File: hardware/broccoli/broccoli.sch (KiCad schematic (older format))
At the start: 82 parts, among them J1 PCB Antenna, J2 USB-MICRO-B, P1 DIGITAL, P11 SCLK, P12 SDAT, P2 PROGRAM, P3 JTAG, P4 EXPAND, P5 ANALOG, P6 VCC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

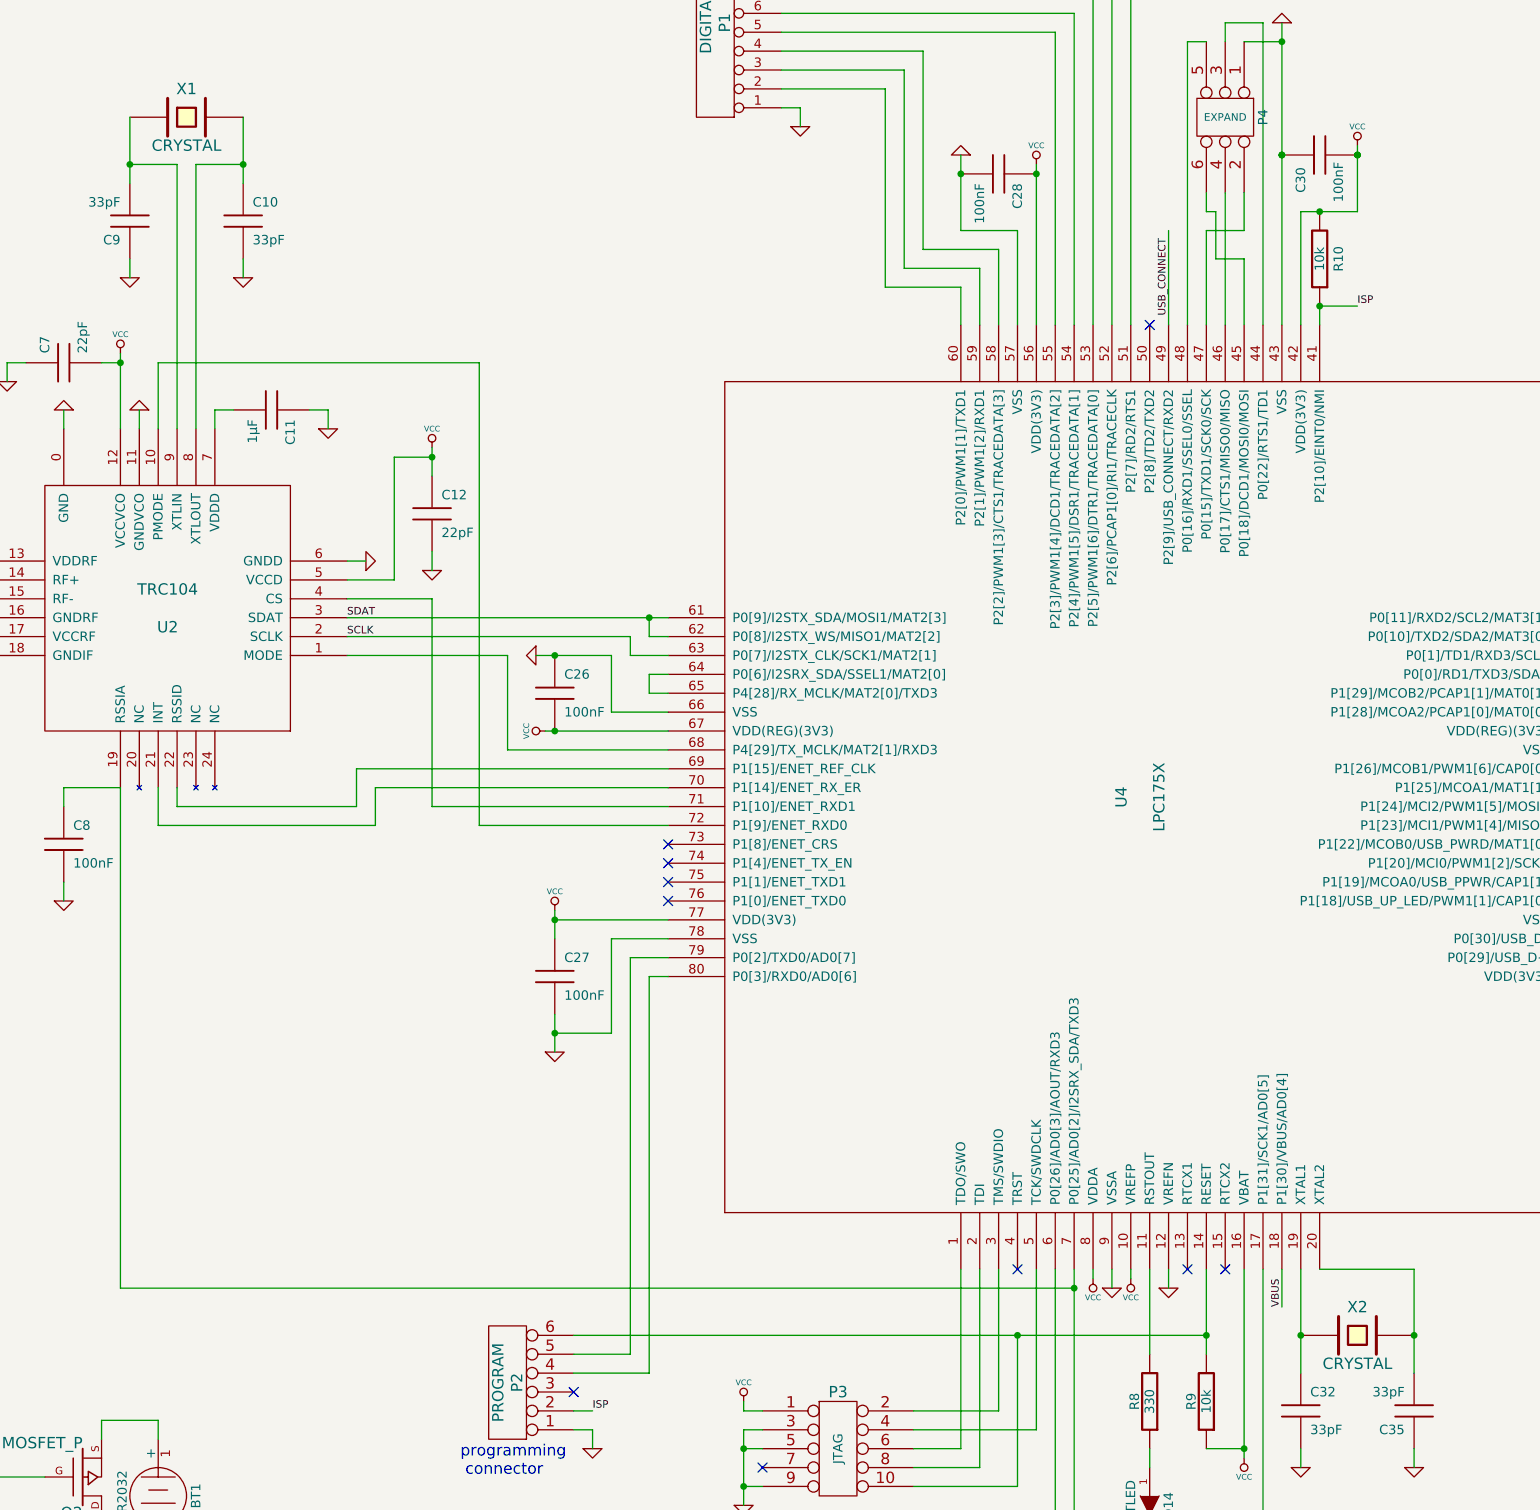
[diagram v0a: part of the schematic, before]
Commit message: Broccoli: replaced some bogus modules
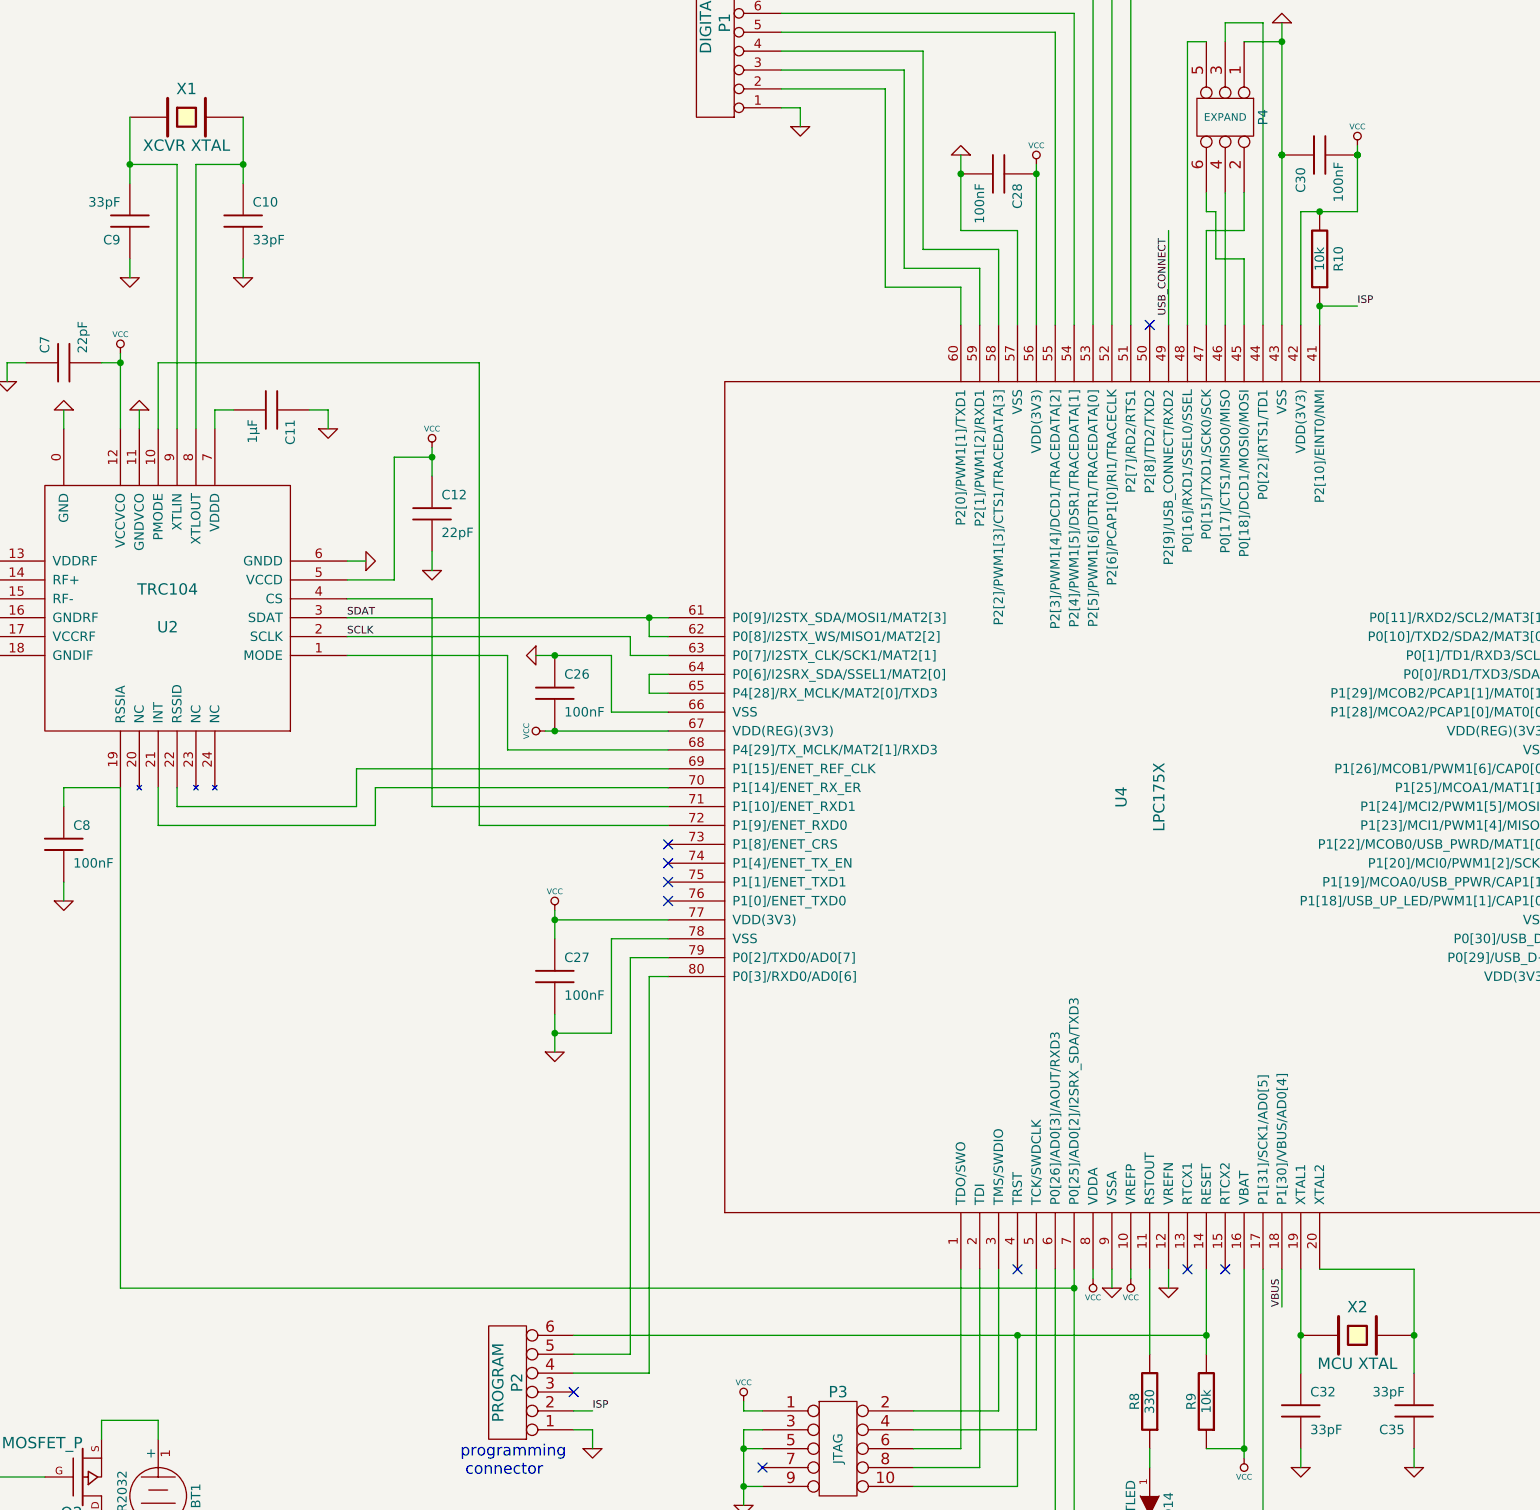
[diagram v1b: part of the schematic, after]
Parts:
- X1: value CRYSTAL -> XCVR XTAL
- X2: value CRYSTAL -> MCU XTAL
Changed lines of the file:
@@
-EESchema Schematic File Version 2  date Sat 13 Aug 2011 10:34:51 PM MDT
+EESchema Schematic File Version 2  date Sun 14 Aug 2011 11:25:26 AM MDT
 LIBS:ubertooth-symbols
 LIBS:power
@@
 P 4750 2000
 F 0 "X1" H 4750 2150 60  0000 C CNN
-F 1 "CRYSTAL" H 4750 1850 60  0000 C CNN
+F 1 "XCVR XTAL" H 4750 1850 60  0000 C CNN
 F 4 "TXC" H 4750 2000 60  0001 C CNN "Field1"
 F 5 "9C-16.000MEEJ-T" H 4750 2000 60  0001 C CNN "Field2"
@@
 P 10950 8450
 F 0 "X2" H 10950 8600 60  0000 C CNN
-F 1 "CRYSTAL" H 10950 8300 60  0000 C CNN
+F 1 "MCU XTAL" H 10950 8300 60  0000 C CNN
 F 4 "TXC" H 10950 8450 60  0001 C CNN "Field1"
 F 5 "9C-16.000MEEJ-T" H 10950 8450 60  0001 C CNN "Field2"

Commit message: Broccoli: grounded antenna
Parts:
- removed J1: PCB Antenna, symbol CONN_1
- added J1: PCB Antenna, symbol BNC
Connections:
- net GND: now also J1.2 (Ext)
- net at C1.2: now also J1.1 (In)
